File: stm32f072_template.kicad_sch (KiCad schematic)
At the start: 23 parts, among them J1 USB_C_Receptacle_USB2.0, J2 Conn_01x20, J3 Conn_01x20, U1 STM32F072CBT6, U2 PRTR5V0U2X

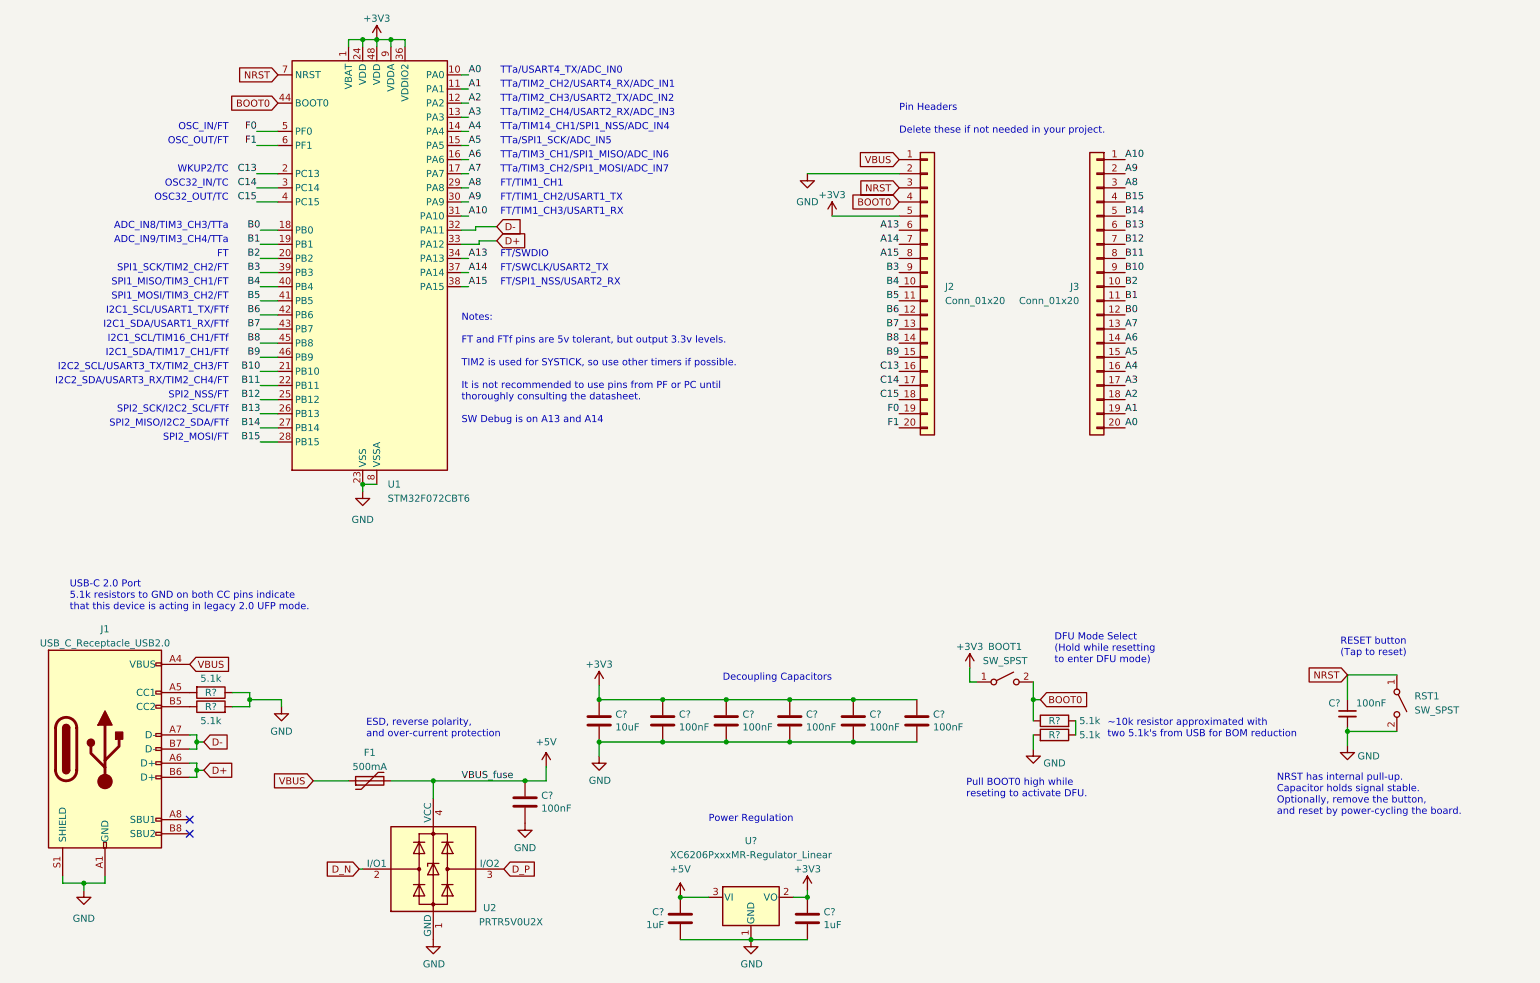
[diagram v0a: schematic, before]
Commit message: Fixed net typos, added notes
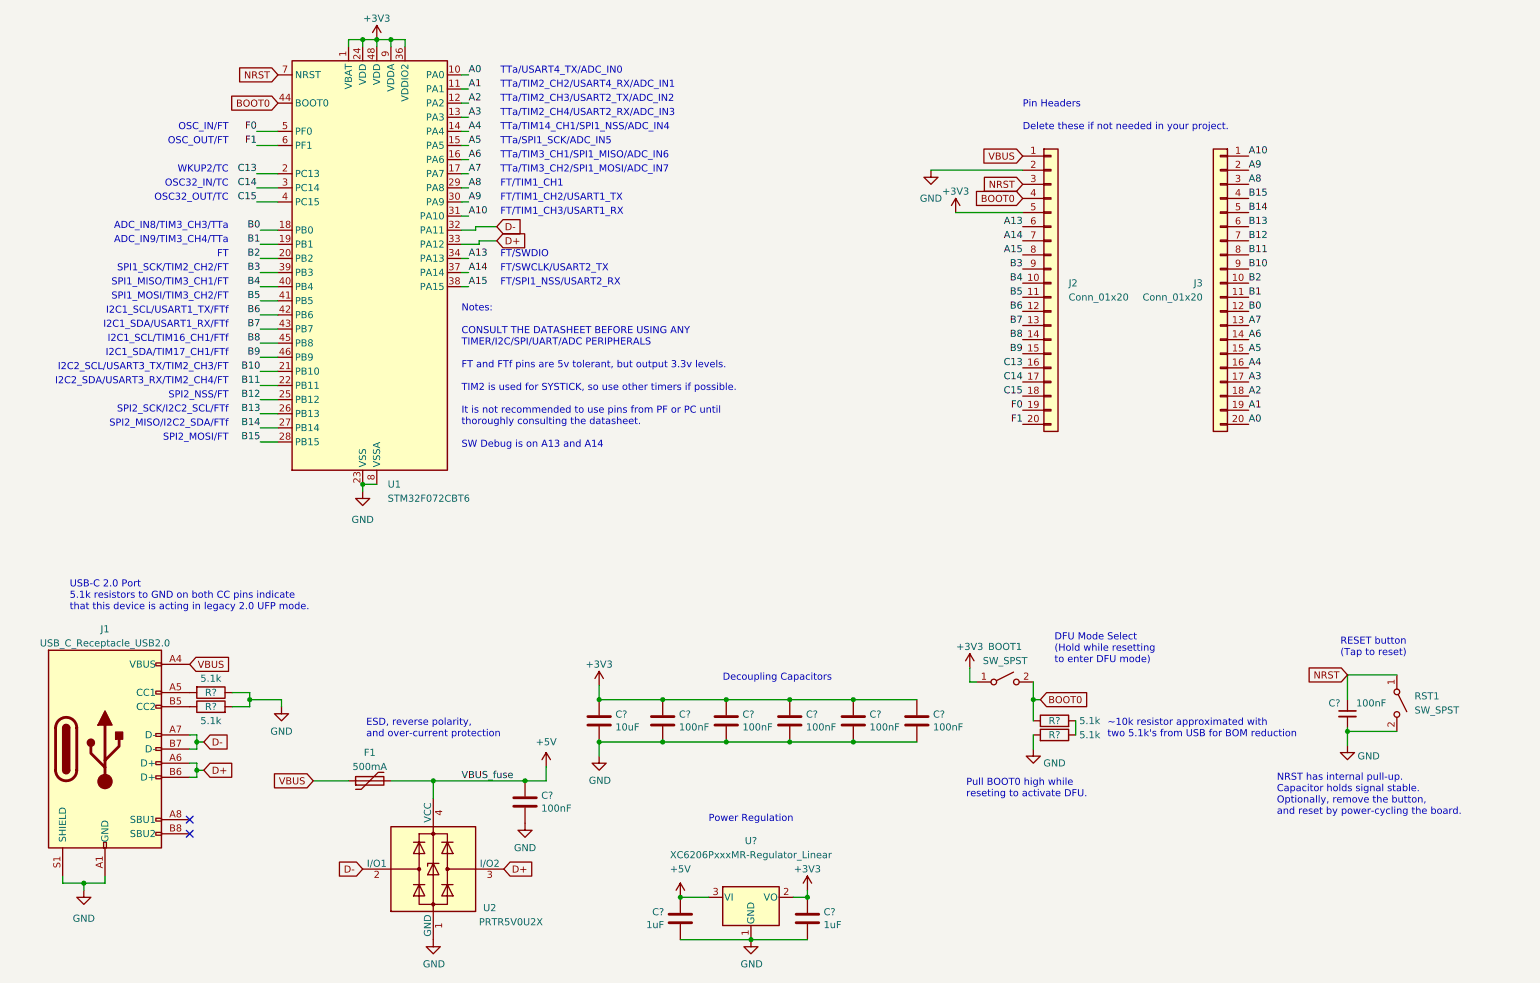
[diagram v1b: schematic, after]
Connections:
- net D_N is gone; now on net D-: U2.2 (I/O1)
- net D_P is gone; now on net D+: U2.3 (I/O2)
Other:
- note added: "Notes: CONSULT THE DATASHEET BEFORE USING ANY TIMER/I2C/SPI/UART/ADC PERIPHERALS FT and FTf pins are 5v tolerant, but output 3.3v levels. TIM2 is used for SYSTICK, so use other timers if possible. It is not recommended to use pins from PF or PC until thoroughly consulting the datasheet. SW Debug is on A13 and A14"
- note removed: "Notes: FT and FTf pins are 5v tolerant, but output 3.3v levels. TIM2 is used for SYSTICK, so use other timers if possible. It is not recommended to use pins from PF or PC until thoroughly consulting the datasheet. SW Debug is on A13 and A14"
- moved on the sheet: J2, J3
